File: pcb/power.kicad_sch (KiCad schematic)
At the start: 24 parts, among them U1 LM27762DSST, U2 NCP1117-2.5_SOT223, U3 LT1790ACS6-1.25

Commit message: pcb layout polishing
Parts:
- TP_1V25, TP_2V5, TP_3V3, TP_NEG_3V3: footprint (none) -> TestPoint:TestPoint_THTPad_D2.0mm_Drill1.0mm
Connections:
- net EXP renamed GND
- net GND: no longer U1.14 (EXP), U1.15 (EXP), U1.16 (EXP)
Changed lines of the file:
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@@
+	(wire
+		(pts
+			(xy 77.47 71.12) (xy 77.47 74.93)
+		)
+		(stroke
+			(width 0)
+			(type default)
+		)
+	)
 	(wire
 		(pts
@@
 		(pts
 			(xy 22.86 46.99) (xy 22.86 48.26)
-		)
-		(stroke
-			(width 0)
-			(type default)
-		)
-	)
-	(wire
-		(pts
-			(xy 77.47 72.39) (xy 77.47 74.93)
 		)
 		(stroke
@@
 			)
 		)
-		(property "Footprint" ""
+		(property "Footprint" "TestPoint:TestPoint_THTPad_D2.0mm_Drill1.0mm"
 			(at 262.89 138.43 0)
 			(effects
@@
 			)
 		)
-		(property "Footprint" ""
+		(property "Footprint" "TestPoint:TestPoint_THTPad_D2.0mm_Drill1.0mm"
 			(at 123.19 92.71 0)
 			(effects
@@
 			)
 		)
-		(property "Footprint" ""
+		(property "Footprint" "TestPoint:TestPoint_THTPad_D2.0mm_Drill1.0mm"
 			(at 260.35 90.17 0)
 			(effects
@@
 		(pin "2"
 		)
-		(pin "15"
-		)
-		(pin "14"
-		)
-		(pin "16"
-		)
 		(instances
 			(project "SensEdu"
@@
 			)
 		)
-		(property "Footprint" ""
+		(property "Footprint" "TestPoint:TestPoint_THTPad_D2.0mm_Drill1.0mm"
 			(at 210.82 90.17 0)
 			(effects

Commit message: in works
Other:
- note added: "3.3 from arduino"
- note added: "features to debug"
- title: SensEdu 0.7 -> SensEdu 0.9
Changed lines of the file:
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@@
 	(paper "A4")
 	(title_block
-		(title "SensEdu 0.7")
+		(title "SensEdu 0.9")
 		(date "2025-12-05")
 		(company "Infineon Technologies")
@@
 		)
 	)
+	(text "features to debug"
+		(exclude_from_sim no)
+		(at 59.69 87.63 0)
+		(effects
+			(font
+				(size 1.27 1.27)
+			)
+		)
+	)
 	(text "LOW DROPOUT VOLTAGE REFERENCE 3.3V->2.5V"
 		(exclude_from_sim yes)
@@
 		)
 	)
+	(text "3.3 from arduino "
+		(exclude_from_sim no)
+		(at 194.31 92.71 0)
+		(effects
+			(font
+				(size 1.27 1.27)
+			)
+		)
+	)
 	(junction
 		(at 109.22 81.28)
@@
 	(wire
 		(pts
-			(xy 204.47 138.43) (xy 220.98 138.43)
+			(xy 210.82 138.43) (xy 220.98 138.43)
 		)
 		(stroke
@@
 	(symbol
 		(lib_id "power:+3.3V")
-		(at 204.47 138.43 0)
+		(at 210.82 138.43 0)
 		(unit 1)
 		(exclude_from_sim no)
@@
 		(dnp no)
 		(property "Reference" "#PWR012"
-			(at 204.47 142.24 0)
+			(at 210.82 142.24 0)
 			(effects
 				(font
@@
 		)
 		(property "Value" "+3.3V"
-			(at 204.47 134.62 0)
+			(at 210.82 134.62 0)
 			(effects
 				(font
@@
 		)
 		(property "Footprint" ""
-			(at 204.47 138.43 0)
+			(at 210.82 138.43 0)
 			(effects
 				(font
@@
 		)
 		(property "Datasheet" ""
-			(at 204.47 138.43 0)
+			(at 210.82 138.43 0)
 			(effects
 				(font
@@
 		)
 		(property "Description" "Power symbol creates a global label with name \"+3.3V\""
-			(at 204.47 138.43 0)
-			(effects
-				(font
+			(at 210.82 138.43 0)
+			(effects
+				(font

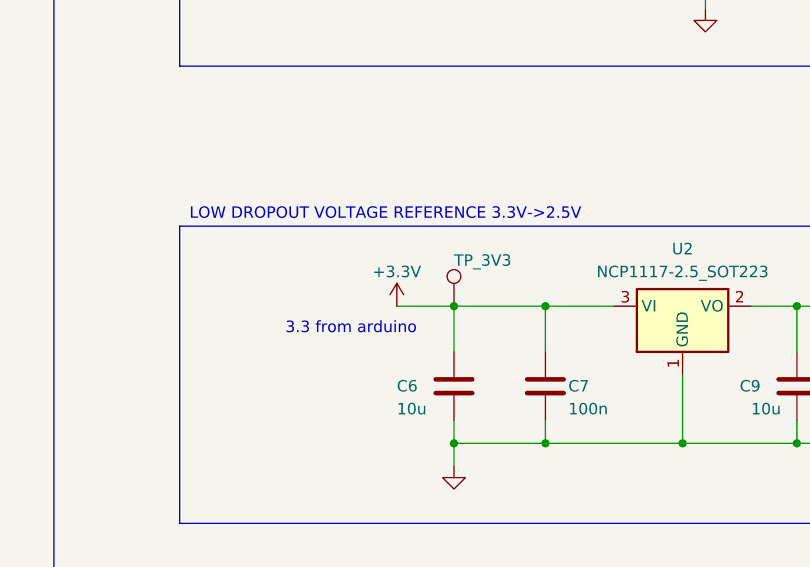
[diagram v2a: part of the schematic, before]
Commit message: fix: PCB final fixes
Added simulation for dc offset after ac coupling
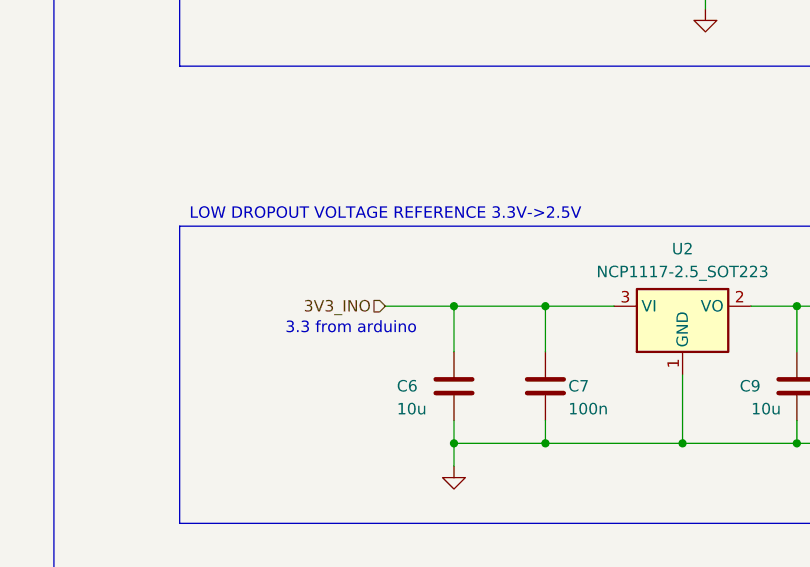
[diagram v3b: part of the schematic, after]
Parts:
- removed TP_3V3: TestPoint, TestPoint:TestPoint_THTPad_D2.0mm_Drill1.0mm, symbol Connector:TestPoint
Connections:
- net +3.3V: no longer C6.1, C7.1, U2.3 (VI)
- new net 3V3_INO: C6.1, C7.1, U2.3 (VI)
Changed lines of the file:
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@@
+	(wire
+		(pts
+			(xy 198.12 90.17) (xy 205.74 90.17)
+		)
+		(stroke
+			(width 0)
+			(type default)
+		)
+	)
 	(wire
 		(pts
@@
 		(pts
 			(xy 77.47 58.42) (xy 95.25 58.42)
-		)
-		(stroke
-			(width 0)
-			(type default)
-		)
-	)
-	(wire
-		(pts
-			(xy 199.39 90.17) (xy 205.74 90.17)
 		)
 		(stroke
@@
 		)
 	)
+	(hierarchical_label "3V3_INO"
+		(shape input)
+		(at 198.12 90.17 180)
+		(effects
+			(font
+				(size 1.27 1.27)
+			)
+			(justify right)
+		)
+	)
 	(symbol
 		(lib_id "Device:C")
@@
 	)
 	(symbol
-		(lib_id "power:+3.3V")
-		(at 199.39 90.17 0)
-		(unit 1)
-		(exclude_from_sim no)
-		(in_bom yes)
-		(on_board yes)
-		(dnp no)
-		(property "Reference" "#PWR011"
-			(at 199.39 93.98 0)
-			(effects
-				(font
-					(size 1.27 1.27)
-				)
-				(hide yes)
-			)
-		)
-		(property "Value" "+3.3V"
-			(at 199.39 86.36 0)
-			(effects
-				(font
-					(size 1.27 1.27)
-				)
-			)
-		)
-		(property "Footprint" ""
-			(at 199.39 90.17 0)
-			(effects
-				(font
-					(size 1.27 1.27)
-				)
-				(hide yes)
-			)
-		)
-		(property "Datasheet" ""
-			(at 199.39 90.17 0)
-			(effects
-				(font
-					(size 1.27 1.27)
-				)
-				(hide yes)
-			)
-		)
-		(property "Description" "Power symbol creates a global label with name \"+3.3V\""
-			(at 199.39 90.17 0)
-			(effects
-				(font
-					(size 1.27 1.27)
-				)
-				(hide yes)
-			)
-		)
-		(pin "1"
-		)
-		(instances
-			(project "SensEdu"
-				(path "/e63e39d7-6ac0-4ffd-8aa3-1841a4541b55/980ab19c-1e73-474b-994e-c8e10885075a"
-					(reference "#PWR011")
-					(unit 1)
-				)
-			)
-		)
-	)
-	(symbol
 		(lib_id "Device:C")
 		(at 243.84 99.06 0)
@@
 					(unit 1)
 				)
-			)
-		)
-	)
-	(symbol
-		(lib_id "Connector:TestPoint")
-		(at 205.74 90.17 0)
-		(unit 1)
-		(exclude_from_sim no)
-		(in_bom yes)
-		(on_board yes)
-		(dnp no)
-		(property "Reference" "TP_3V3"
-			(at 205.74 85.09 0)
-			(effects
-				(font
-					(size 1.27 1.27)
-				)
-				(justify left)
-			)
-		)
-		(property "Value" "TestPoint"
-			(at 208.28 88.1379 0)
-			(effects
-				(font
-					(size 1.27 1.27)
-				)
-				(justify left)
-				(hide yes)
-			)
-		)
-		(property "Footprint" "TestPoint:TestPoint_THTPad_D2.0mm_Drill1.0mm"
-			(at 210.82 90.17 0)
-			(effects
-				(font
-					(size 1.27 1.27)
-				)
-				(hide yes)
-			)
-		)
-		(property "Datasheet" "~"
-			(at 210.82 90.17 0)
-			(effects
-				(font
-					(size 1.27 1.27)
-				)
-				(hide yes)
-			)
-		)
-		(property "Description" "test point"
-			(at 205.74 90.17 0)
-			(effects
-				(font
-					(size 1.27 1.27)
-				)
-				(hide yes)
-			)
-		)
-		(pin "1"
-		)
-		(instances
-			(project "SensEdu"
-				(path "/e63e39d7-6ac0-4ffd-8aa3-1841a4541b55/980ab19c-1e73-474b-994e-c8e10885075a"
-					(reference "TP_3V3")
-					(unit 1)
-				)

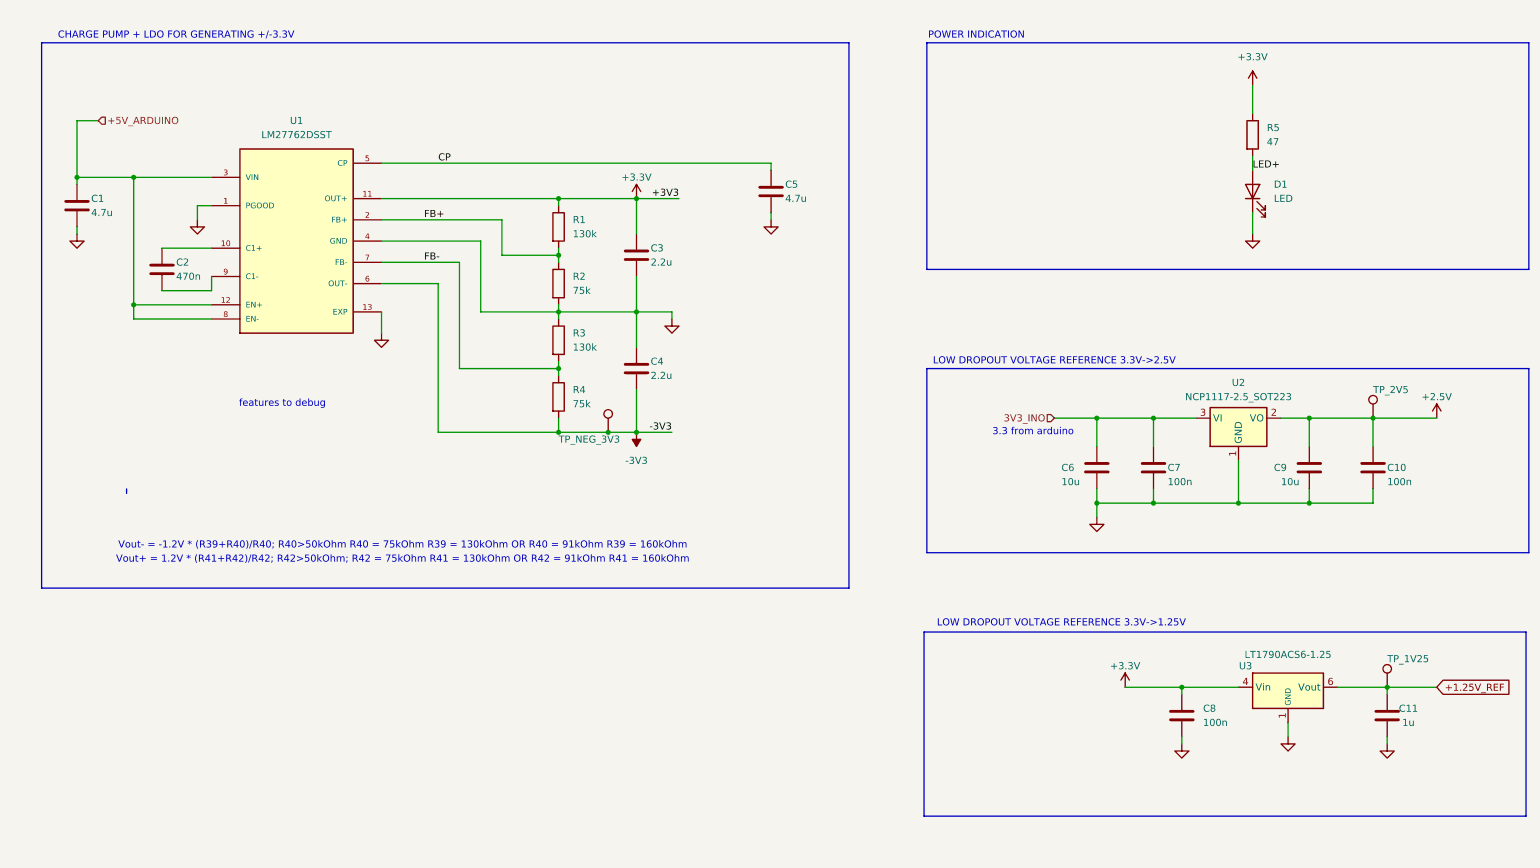
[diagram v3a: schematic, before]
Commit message: feat: Redraw PCB layout
- Change supply polarity and pin numbers of ADA4511
- Change cap of switches to 100n to reduce bom
- Change supply of sensors to unison 3.3V
- Rearrange mic and amps pins
- Add mountains
- Add Infineon logo
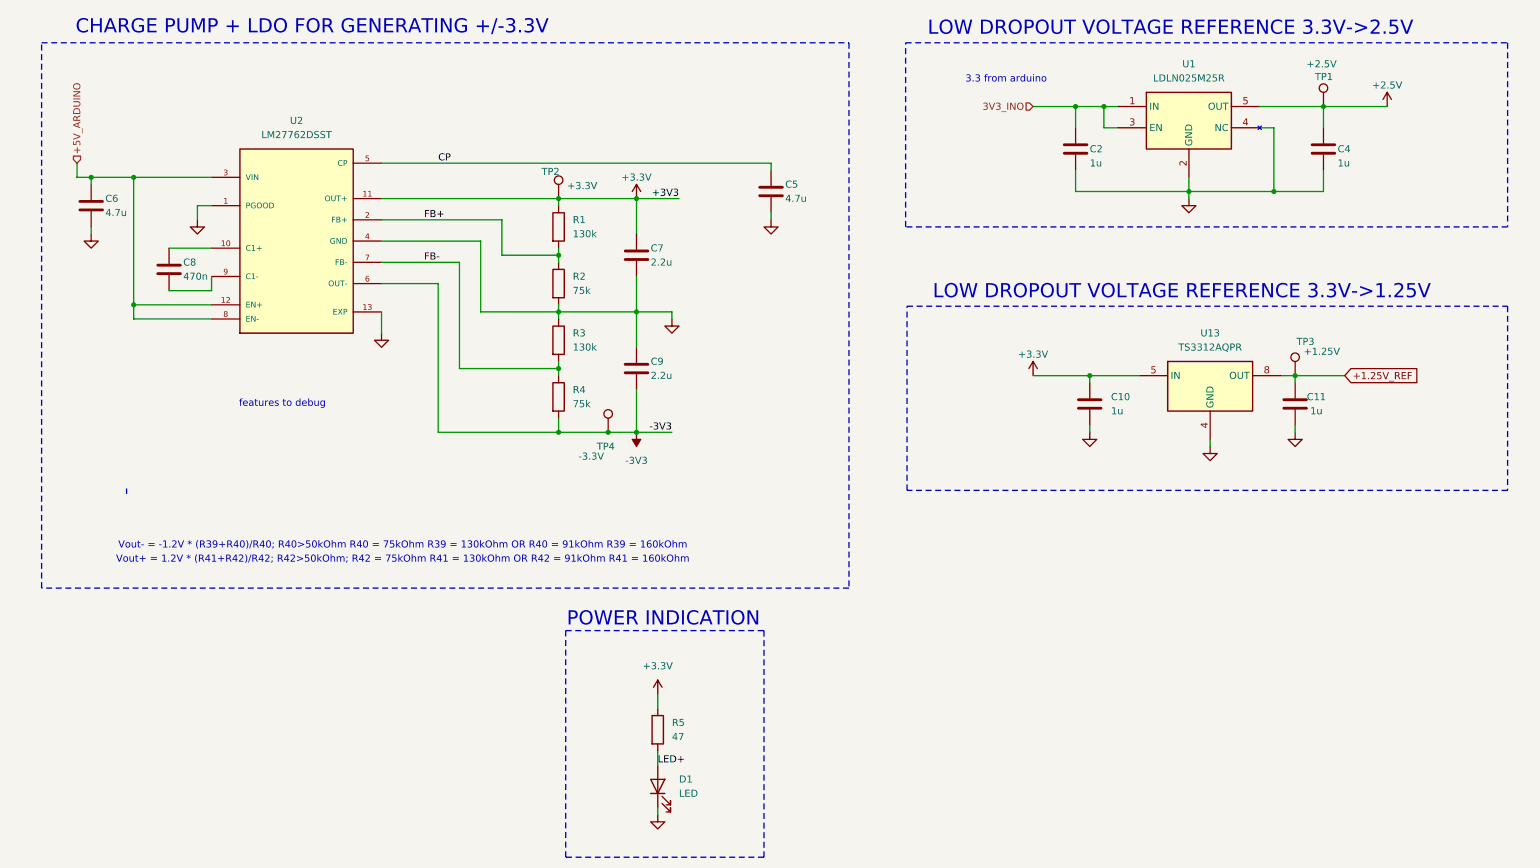
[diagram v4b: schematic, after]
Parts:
- removed C6, C9: 10u, Capacitor_SMD:C_0805_2012Metric, symbol Device:C
- removed U2: NCP1117-2.5_SOT223, Package_TO_SOT_SMD:SOT-223-3_TabPin2, symbol Regulator_Linear:NCP1117-2.5_SOT223
- removed U3: LT1790ACS6-1.25, Package_TO_SOT_SMD:TSOT-23-6, symbol SensEdu:LT1790-2.5_sensedu
- added TP2: +3.3V, TestPoint:TestPoint_THTPad_D2.0mm_Drill1.0mm, symbol SensEdu:TestPoint
- added U1: LDLN025M25R, SamacSys_Parts:SOT95P280X145-5N, symbol SensEdu:LDLN025M25R
- added U13: TS3312AQPR, SamacSys_Parts:TS3312AQPR, symbol SensEdu:TS3312AQPR
- C10: renamed from C8; value 100n -> 1u; footprint Capacitor_SMD:C_0805_2012Metric -> Capacitor_SMD:C_0603_1608Metric; symbol Device:C -> SensEdu:C
- C11: footprint Capacitor_SMD:C_0805_2012Metric -> Capacitor_SMD:C_0603_1608Metric; symbol Device:C -> SensEdu:C
- C2: renamed from C7; value 100n -> 1u; footprint Capacitor_SMD:C_0805_2012Metric -> Capacitor_SMD:C_0603_1608Metric; symbol Device:C -> SensEdu:C
- C4: renamed from C10; value 100n -> 1u; footprint Capacitor_SMD:C_0805_2012Metric -> Capacitor_SMD:C_0603_1608Metric; symbol Device:C -> SensEdu:C
- C5: symbol Device:C -> SensEdu:C
- C6: renamed from C1; symbol Device:C -> SensEdu:C
- C7: renamed from C3; symbol Device:C -> SensEdu:C
- C8: renamed from C2; footprint Capacitor_SMD:C_0805_2012Metric -> Capacitor_SMD:C_0603_1608Metric; symbol Device:C -> SensEdu:C
- C9: renamed from C4; symbol Device:C -> SensEdu:C
- D1: symbol Device:LED -> SensEdu:LED
- R1, R2, R3, R4, R5: footprint Resistor_SMD:R_0805_2012Metric -> Resistor_SMD:R_0603_1608Metric; symbol Device:R -> SensEdu:R
- TP1: renamed from TP_2V5; value TestPoint -> +2.5V; symbol Connector:TestPoint -> SensEdu:TestPoint
- TP3: renamed from TP_1V25; value TestPoint -> +1.25V; symbol Connector:TestPoint -> SensEdu:TestPoint
- TP4: renamed from TP_NEG_3V3; value TestPoint -> -3.3V; symbol Connector:TestPoint -> SensEdu:TestPoint
- renumbered U1 to U2
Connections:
- net +1.25V_REF: now also U13.8 (OUT)
- net +2.5V: now also U1.5 (OUT)
- net +3.3V: now also TP2.1, U13.5 (IN)
- net 3V3_INO: now also U1.1 (IN), U1.3 (EN)
- net GND: now also U1.2 (GND), U1.4 (NC), U13.4 (GND)
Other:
- title: SensEdu 0.9 -> SensEdu
- moved on the sheet: C10, C11, C2, C4, C6, C8, D1, R5, TP1, TP3
